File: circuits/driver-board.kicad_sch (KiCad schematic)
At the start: 59 parts, among them J1 Backpack_Conn_02x09, J2 USB4120-03-C_REVA, J3 Motor_Conn_01x04, Q1 MMBT3904, Q2 MMBT3904, SW1 ESP_EN_SW_Push, SW2 ESP_IO0_SW_Push, U1 CP2102N-A01-GQFN24, U2 BD33FC0WEFJ-E2, U3 ESP32-S3, U4 AS5601-ASOT, U5 TMC2209-LA, U6 STUSB4500QTR

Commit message: updated 3d models
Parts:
- removed U2: BD33FC0WEFJ-E2, Slimc_Converter_DCDC:BD33FC0WEFJ-E2, symbol Slimc_Converter_DCDC:BD33FC0WEFJ-E2
- added U2: BAxxXX0, Package_TO_SOT_SMD:TO-252-2, symbol Slimc_Converter_DCDC:BAxxXX0
- gave numbers to parts that had none: 1
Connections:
- net +3V3: now also U2.3 (OUT)
- net VBUS: now also U2.1 (VCC)
- new net: U2.2 (GND), U2.Fin (GND)
- no-connect marks 35 -> 30
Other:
- moved on the sheet: C3

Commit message: work on external spram and pcb layout
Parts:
- removed AE1: Antenna_Shield, symbol Device:Antenna_Shield
- removed C2: ??µF 35V, Capacitor_SMD:C_1206_3216Metric, symbol Device:CP_Small
- removed C24: 100µF-6.3V-0603, Capacitor_SMD:C_0603_1608Metric, symbol Device:CP_Small
- removed C6: 100nF, Capacitor_SMD:C_0603_1608Metric, symbol Device:CP_Small
- removed C7: 2µ2F-6.3V, Capacitor_SMD:C_0603_1608Metric, symbol Device:C_Small
- removed J1: Backpack_Conn_02x09, Connector_PinSocket_2.54mm:PinSocket_2x09_P2.54mm_Vertical, symbol Connector:Screw_Terminal_01x18
- removed J4: Barrel_Jack, symbol Connector:Barrel_Jack
- removed R3: 4K7-0402, Resistor_SMD:R_0603_1608Metric, symbol Device:R_Small
- removed SW2: ESP_IO0_SW_Push, Button_Switch_SMD:SW_SPST_B3U-1000P, symbol Switch:SW_Push
- added AE1: Antenna, Slimc_RF_Antenna:XCVR_NN01-102, symbol Device:Antenna
- added C2, C24, C26, C27, C28: 1µF-6v3, Capacitor_SMD:C_0402_1005Metric, symbol Device:C_Small
- added C29: 0.1µF-6v3, Capacitor_SMD:C_0402_1005Metric, symbol Device:C_Small
- added C6: 100nF-6v3-0603, Capacitor_SMD:C_0402_1005Metric, symbol Device:C_Small
- added J1: Conn_01x18_Female, Connector_PinSocket_2.54mm:PinSocket_2x09_P2.54mm_Vertical, symbol Connector:Conn_01x18_Female
- added J4: Screw_Terminal_01x02, TerminalBlock_Phoenix:TerminalBlock_Phoenix_MKDS-1,5-2-5.08_1x02_P5.08mm_Horizontal, symbol Connector:Screw_Terminal_01x02
- added J5: Conn_01x06_Female, Connector_PinSocket_2.54mm:PinSocket_2x03_P2.54mm_Vertical, symbol Connector:Conn_01x06_Female
- added R14: 4K7-0402, Resistor_SMD:R_0402_1005Metric, symbol Device:R_Small
- added R2: 20K-0402, Resistor_SMD:R_0402_1005Metric, symbol Device:R_Small
- added R5: 715K-0402, Resistor_SMD:R_0402_1005Metric, symbol Device:R_Small
- added R6: 110K-0402, Resistor_SMD:R_0402_1005Metric, symbol Device:R_Small
- added R9: 100K-0402, Resistor_SMD:R_0402_1005Metric, symbol Device:R_Small
- added U7: ESP-PSRAM32, Package_SO:SOIC-8_3.9x4.9mm_P1.27mm, symbol Memory_RAM:ESP-PSRAM32
- added Y1: 40Mhz, Crystal:Crystal_SMD_2016-4Pin_2.0x1.6mm, symbol Device:Crystal_GND2
- C1: value 100nF-6.3V-0603 -> 100nF-6v3-0603; footprint Capacitor_SMD:C_0603_1608Metric -> Capacitor_SMD:C_0402_1005Metric
- C10, C11, C18, C21: footprint Capacitor_SMD:C_0603_1608Metric -> Capacitor_SMD:C_0402_1005Metric
- C14, C15, C16, C17: footprint Capacitor_SMD:C_0603_1608Metric -> Capacitor_SMD:C_0402_1005Metric; now left out of the parts list
- C20: footprint (none) -> Capacitor_SMD:C_0402_1005Metric
- C25: value TBD -> 1µF-6v3; footprint (none) -> Capacitor_SMD:C_0402_1005Metric
- C3: value ??µF-0603 -> 10µF-35V-0603; footprint Capacitor_SMD:C_0603_1608Metric -> Capacitor_SMD:C_0402_1005Metric
- C4: value 10µF-0603 -> 1µF-6v3-0603; footprint Capacitor_SMD:C_0603_1608Metric -> Capacitor_SMD:C_0402_1005Metric
- C5: value 2µ2F-6.3V -> 0.1µF-6v3; footprint Capacitor_SMD:C_0603_1608Metric -> Capacitor_SMD:C_0402_1005Metric
- C9: value 2µ2F-6.3V -> 2µ2F-6v3; footprint Capacitor_SMD:C_0603_1608Metric -> Capacitor_SMD:C_0402_1005Metric
- D1: footprint Slimc_LED_SMD:WS2812_4020_SIDE -> Slimc_LED_SMD:LED_WS2812C-2020
- H1, H2, H3, H4, Q1, Q2, U1, U6: now left out of the parts list
- R1: value 4K7-0402 -> 10K-0402; footprint Resistor_SMD:R_0603_1608Metric -> Resistor_SMD:R_0402_1005Metric
- R10, R11, R4, R7, R8: footprint Resistor_SMD:R_0603_1608Metric -> Resistor_SMD:R_0402_1005Metric
- R12, R13: value 0R11-2010-1W -> 0R11-0805-1W; footprint Resistor_SMD:R_2010_5025Metric -> Resistor_SMD:R_0805_2012Metric
- R15, R16, R17: footprint Resistor_SMD:R_0603_1608Metric -> Resistor_SMD:R_0402_1005Metric; now left out of the parts list
- SW1: value ESP_EN_SW_Push -> RST_SW_Push
- U2: value BAxxXX0 -> BA33DD0T
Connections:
- net ESP_IO10 is gone; now on net AS5601_ABI_A: U3.15 (GPIO10/ADC1_CH9)
- net +3V3: now also C5.2, R1.1, R7.2, C24.2, C6.2, J5.2 (Pin_2); no longer R1.2, R7.1
- net AS5601_ABI_A: no longer R10.2, R11.1, R11.2, R7.2, R8.2, U1.20 (RXD), U1.21 (TXD), U4.5 (B), U4.6 (SDA), U4.7 (SCL), U5.11 (DIAG), U5.14 (PDN_UART), U5.16 (STEP), U5.19 (DIR), U5.2 (ENN), U6.7 (SCL), U6.8 (SDA)
- net ESP_EN: now also R1.2, SW1.2, C2.1, J5.4 (Pin_4); no longer C5.1, R1.1, SW1.1
- net ESP_IO00: now also J5.3 (Pin_3); no longer U3.52 (GPIO46)
- net ESP_IO04: now also R10.2, U4.7 (SCL), U6.7 (SCL), J1.16 (Pin_16)
- net ESP_IO05: now also R8.2, U4.6 (SDA), U6.8 (SDA), J1.15 (Pin_15)
- net ESP_IO06: now also R7.1, U5.2 (ENN), J1.14 (Pin_14)
- net ESP_IO07: now also U5.11 (DIAG), R2.1
- net ESP_IO08: now also U5.16 (STEP)
- net ESP_IO09: now also U5.19 (DIR)
- net ESP_IO14: now also J1.12 (Pin_12), R5.2, R6.1
- net ESP_IO17: now also J1.11 (Pin_11)
- net ESP_IO18: now also J1.10 (Pin_10)
- net ESP_IO19: now also J1.9 (Pin_9)
- net ESP_IO43: now also U1.21 (TXD), J5.6 (Pin_6)
- net ESP_IO44: now also U1.20 (RXD), J5.5 (Pin_5)
- net ESP_IO45: now also R11.1, J1.18 (Pin_18)
- net GND: now also C5.1, C9.2, L1.1, SW1.1, U2.2 (GND), U2.Fin (GND), C2.2, C24.1, C26.1, C27.1, C28.1, C29.1, C6.1, J1.1 (Pin_1), J1.13 (Pin_13), J1.3 (Pin_3), J1.5 (Pin_5), J4.1 (Pin_1), J5.1 (Pin_1), R14.1, R2.2, R6.2, U7.4 (VSS), Y1.2; no longer C20.2, C5.2, C9.1, SW1.2
- net VBUS: now also J1.2 (Pin_2), J1.4 (Pin_4), J1.6 (Pin_6), J4.2 (Pin_2), R5.1
- net at U5.8 (5VOUT): now also C9.1; no longer C9.2
- net at L1.2: now also C20.1, AE1.1 (A); no longer C25.2
- net ESP_SPICS1: now reaches U3.28 (SPI_CS1/GPIO26)
- net ESP_SPICS1: now also R9.2, U7.1 (~{CE})
- net ESP_SPIVDD: now reaches U3.29 (VDD_SPI)
- net ESP_SPIVDD: now also C28.2, C29.2, R9.1, U7.8 (VCC)
- net ESP_SPIHD: now reaches U3.30 (SPIHD/GPIO27)
- net ESP_SPIHD: now also U7.7 (SIO3)
- net ESP_SPIWP: now reaches U3.31 (SPIWP/GPIO28)
- net ESP_SPIWP: now also U7.3 (SIO2)
- net ESP_SPICLK: now reaches U3.33 (SPICLK/GPIO30)
- net ESP_SPICLK: now also U7.6 (SCLK)
- net ESP_SPIQ: now reaches U3.34 (SPIQ/GPIO31)
- net ESP_SPIQ: now also U7.2 (SO/SIO)
- net ESP_SPID: now reaches U3.35 (SPID/GPIO32)
- net ESP_SPID: now also U7.5 (SI/SIO)
- net at U3.37 (SPICLK_P/GPIO47): now also C27.2, R14.2
- net at U3.53 (XTAL_N): now also C26.2, Y1.3
- net at U3.54 (XTAL_P): now also C25.2, Y1.1
- net ESP_IO11 renamed AS5601_ABI_B
- net AS5601_ABI_B: now also U4.5 (B)
- new net: C20.2, U3.1 (LNA_IN/RF)
- new net ESP_IO46: J1.17 (Pin_17), R11.2, U3.52 (GPIO46), U5.14 (PDN_UART)
- no-connect marks 30 -> 20
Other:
- note added: "2) CLC filter on analog power pins https://www.espressif.com/sites/default/files/documentation/esp32-s3_hardware_design_guidelines_en.pdf#page=8"
- note added: "3) External clock https://www.espressif.com/sites/default/files/documentation/esp32-s3_hardware_design_guidelines_en.pdf#page=11"
- note added: "Delay boot ~50µS"
- note added: "MAX 25V"
- note added: "MAX 5A LOAD"
- note added: "PROGRAMMING HEADER"
- note added: "TO BE DELETED"
- note added: "USB TO UART"
- note added: "from https://dl.espressif.com/dl/SCH_ESP32-S3-DEVKITC-1_V1_20210312C.pdf"
- note removed: "USB TO UART (from https://dl.espressif.com/dl/SCH_ESP32-S3-DEVKITC-1_V1_20210312C.pdf)"
- moved on the sheet: C14, C15, C16, C17, C18, C19, C20, C21, C22, C23, C3, C4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

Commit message: couple of renders
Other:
- note removed: "1) Adding GPIO46 to reset circuitry according to TABLE 9: Strapping Pins https://www.espressif.com/sites/default/files/documentation/esp32-s3_datasheet_en.pdf#page=22"
- note removed: "2) CLC filter on analog power pins https://www.espressif.com/sites/default/files/documentation/esp32-s3_hardware_design_guidelines_en.pdf#page=8"
- note removed: "3) External clock https://www.espressif.com/sites/default/files/documentation/esp32-s3_hardware_design_guidelines_en.pdf#page=11"
- note removed: "NOTES"
- note removed: "TO BE DELETED"
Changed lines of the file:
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@@
-    (stroke (width 0) (type default) (color 0 0 0 0))
-  )
-  (polyline (pts (xy 382.27 405.13) (xy 382.27 303.53))
     (stroke (width 0) (type default) (color 0 0 0 0))
   )
@@
     (stroke (width 0) (type default) (color 0 0 0 0))
   )
-  (polyline (pts (xy 16.51 303.53) (xy 16.51 405.13))
-    (stroke (width 0) (type default) (color 0 0 0 0))
-  )
   (wire (pts (xy 173.99 59.055) (xy 173.99 77.47))
     (stroke (width 0) (type default) (color 0 0 0 0))
@@
   )
   (wire (pts (xy 230.505 264.16) (xy 234.95 264.16))
-    (stroke (width 0) (type default) (color 0 0 0 0))
-  )
-  (polyline (pts (xy 16.51 405.13) (xy 382.27 405.13))
     (stroke (width 0) (type default) (color 0 0 0 0))
   )
@@
   )
   (text "MAX 5A LOAD" (at 471.805 203.835 90)
-    (effects (font (size 1.27 1.27)) (justify left bottom))
-  )
-  (text "NOTES" (at 17.78 307.34 0)
     (effects (font (size 1.27 1.27)) (justify left bottom))
   )
@@
     (effects (font (size 2.54 2.54) (thickness 0.508) bold) (justify left bottom))
   )
-  (text "1) Adding GPIO46 to reset circuitry according to TABLE 9: Strapping Pins https://www.espressif.com/sites/default/files/documentation/esp32-s3_datasheet_en.pdf#page=22"
-    (at 20.32 312.42 0)
-    (effects (font (size 1.27 1.27)) (justify left bottom))
-  )
   (text "STATUS LED" (at 383.54 85.725 0)
     (effects (font (size 2.54 2.54) (thickness 0.508) bold) (justify left bottom))
   )
-  (text "2) CLC filter on analog power pins https://www.espressif.com/sites/default/files/documentation/esp32-s3_hardware_design_guidelines_en.pdf#page=8"
-    (at 20.32 316.23 0)
-    (effects (font (size 1.27 1.27)) (justify left bottom))
-  )
   (text "STEPPER CONTROL" (at 158.115 22.86 0)
     (effects (font (size 2.54 2.54) (thickness 0.508) bold) (justify left bottom))
@@
     (effects (font (size 2.54 2.54) (thickness 0.508) bold) (justify left bottom))
   )
-  (text "TO BE DELETED" (at 384.175 309.245 0)
-    (effects (font (size 2.54 2.54) (thickness 0.508) bold) (justify left bottom))
-  )
-  (text "3) External clock https://www.espressif.com/sites/default/files/documentation/esp32-s3_hardware_design_guidelines_en.pdf#page=11"
-    (at 20.32 320.04 0)
-    (effects (font (size 1.27 1.27)) (justify left bottom))
-  )
   (text "Delay boot ~50µS" (at 211.455 197.485 0)

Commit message: adjusting schematic and pcb component placement
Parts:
- removed C24: 1µF-6v3, Capacitor_SMD:C_0402_1005Metric, symbol Device:C_Small
- removed Q1, Q2: MMBT3904, Package_TO_SOT_SMD:SOT-23, symbol Transistor_BJT:MMBT3904
- removed Y1: 40Mhz, Crystal:Crystal_SMD_2016-4Pin_2.0x1.6mm, symbol Device:Crystal_GND2
- added C30: 1µF, Capacitor_SMD:C_0402_1005Metric, symbol Device:C_Small
- added C31, C32, C33: 100nF, Capacitor_SMD:C_0402_1005Metric, symbol Device:C_Small
- added C34: 1pF, Capacitor_SMD:C_0402_1005Metric, symbol Device:C_Small
- added C35: 15pF, Capacitor_SMD:C_0402_1005Metric, symbol Device:C_Small
- added C7: 10nF, Capacitor_SMD:C_0402_1005Metric, symbol Device:C_Small
- added Q1, Q2: SS8050-G, Package_TO_SOT_SMD:SOT-23, symbol Device:Q_NPN_BEC
- added R3: 20K, Resistor_SMD:R_0402_1005Metric, symbol Device:R_Small
- added U8: 74LVC2G00, Package_SON:X2SON-8_1.4x1mm_P0.35mm, symbol 74xGxx:74LVC2G00
- added Y1: 40MHz, Crystal:Crystal_SMD_2016-4Pin_2.0x1.6mm, symbol Device:Crystal_GND24
- AE1: symbol Device:Antenna -> Device:Antenna_Shield
- C1, C6: value 100nF-6v3-0603 -> 100nF
- C12, C13: value 100nF-16V -> 100nF
- C18: value 100nF-25V -> 100nF
- C2, C27, C28: value 1µF-6v3 -> 1µF
- C20: value TBD -> NC
- C21: value 100nF-50V-0603 -> 100nF-50V
- C22, C23: value 10µF-50V-2220 -> 10µF-50V
- C25: value 1µF-6v3 -> 10µF
- C26: value 1µF-6v3 -> 15pF
- C29: value 0.1µF-6v3 -> 100nF
- C3: value 10µF-35V-0603 -> 10µF-35V
- C4: value 1µF-6v3-0603 -> 1µF
- C5: value 0.1µF-6v3 -> 1µF
- D3: value SMB28A -> SMB24A; footprint Diode_SMD:D_SMB -> Diode_SMD:D_1210_3225Metric
- J4: value Screw_Terminal_01x02 -> Screw_Terminals
- L1: value TBD -> 0R; footprint (none) -> Resistor_SMD:R_0402_1005Metric
- R1, R15: value 10K-0402 -> 10K
- R10, R14, R8: value 4K7-0402 -> 4K7
- R11: value 1K-1%-0603 -> 1K-1%
- R16, R17: value 10K-0603 -> 10K
- R2, R7: value 20K-0402 -> 20K
- R4: value 230R-0402 -> 230
- R5: value 715K-0402 -> 715K
- R6: value 110K-0402 -> 110K
- R9: value 100K-0402 -> 100K
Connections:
- net ESP_IO12 is gone; now on net AS5601_ABI_B: U3.17 (GPIO12/ADC2_CH1)
- net ESP_IO20 is gone; now on net USB_D+: U3.26 (GPIO20/USB_D+/ADC2_CH9)
- net ESP_IO48 is gone; now on net ESP_IO01: R4.1
- net +3V3: now also C25.2, C30.2, C31.2, C32.2, C33.2, C7.2, R3.1, U8.8 (VCC), U8.8 (VCC)
- net AS5601_ABI_A: now also U3.16 (GPIO11/ADC2_CH0); no longer U3.15 (GPIO10/ADC1_CH9)
- net AS5601_ABI_B: no longer U3.16 (GPIO11/ADC2_CH0)
- net ESP_EN: now also Q1.3 (C)
- net ESP_IO00: now also Q2.3 (C)
- net ESP_IO02: now also J1.8 (Pin_8)
- net ESP_IO03: now also J1.7 (Pin_7)
- net ESP_IO07: now also U5.16 (STEP); no longer R2.1, U5.11 (DIAG)
- net ESP_IO08: now also U5.19 (DIR); no longer U5.16 (STEP)
- net ESP_IO09: now also U8.5, U8.7; no longer U5.19 (DIR)
- net ESP_IO19: no longer U3.25 (GPIO19/USB_D-/ADC2_CH8)
- net ESP_IO44: no longer U3.50 (U0RXD/PROG/GPIO44)
- net GND: now also AE1.2 (Shield), C20.2, C30.1, C31.1, C32.1, C33.1, C34.2, C35.1, C7.1, U8.4 (GND), U8.4 (GND), Y1.2, Y1.4; no longer L1.1
- net USB_D-: now also U3.25 (GPIO19/USB_D-/ADC2_CH8)
- net CP2102_DTR: now reaches R16.1
- net CP2102_DTR: now also U1.23 (DTR), Q2.2 (E); no longer U1.19 (RTS)
- net CP2102_RTS: now reaches R17.1
- net CP2102_RTS: now also U1.19 (RTS), Q1.2 (E); no longer U1.23 (DTR)
- net at R17.2: now also Q2.1 (B)
- net at R16.2: now also Q1.1 (B)
- net at C20.1, L1.2: now also U3.1 (LNA_IN/RF); no longer AE1.1 (A)
- net ESP_XTAL_N: now reaches C26.2, U3.53 (XTAL_N)
- net ESP_XTAL_N: now also Y1.3
- net ESP_XTAL_P: now reaches U3.54 (XTAL_P)
- net ESP_XTAL_P: now also C35.2, Y1.1; no longer C25.2
- net ESP_IO15: no longer names the net of U3.21 (GPIO15/ADC2_CH4/XTAL_32K_P)
- net ESP_IO16: no longer names the net of U3.22 (GPIO16/ADC2_CH5/XTAL_32K_N)
- net ESP_IO33: no longer names the net of U3.38 (GPIO33)
- net ESP_IO34: no longer names the net of U3.39 (GPIO34)
- net ESP_IO35: no longer names the net of U3.40 (GPIO35)
- net ESP_IO36: no longer names the net of U3.41 (GPIO36)
- net ESP_IO37: no longer names the net of U3.42 (GPIO37)
- net ESP_IO38: no longer names the net of U3.43 (GPIO38)
- net ESP_IO39: no longer names the net of U3.44 (MTCK/JTAG/GPIO39)
- net ESP_IO40: no longer names the net of U3.45 (MTDO/JTAG/GPIO40)
- net ESP_IO41: no longer names the net of U3.47 (MTDI/JTAG/GPIO41)
- net ESP_IO42: no longer names the net of U3.48 (MTMS/JTAG/GPIO42)
- new net: AE1.1 (A), C34.1, L1.1
- new net: U8.2, U8.3
- new net ESP_IO10: R3.2, U3.15 (GPIO10/ADC1_CH9), U8.6
- new net TMC2209_DIAG: R2.1, U5.11 (DIAG), U8.1
- no-connect marks 20 -> 32
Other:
- note added: "LET STUSB4500 enable BA33DD0T?"
- note added: "Program Sequence DTR RTS --> EN IO00 1 1 1 1 0 0 1 1 1 0 0 1 0 1 1 0"
- note added: "USB-UART BRIDGE"
- note removed: "USB TO UART"
- moved on the sheet: C12, C13, C20, C26, C27, C3, C4, H1, H2, H3, H4, J1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

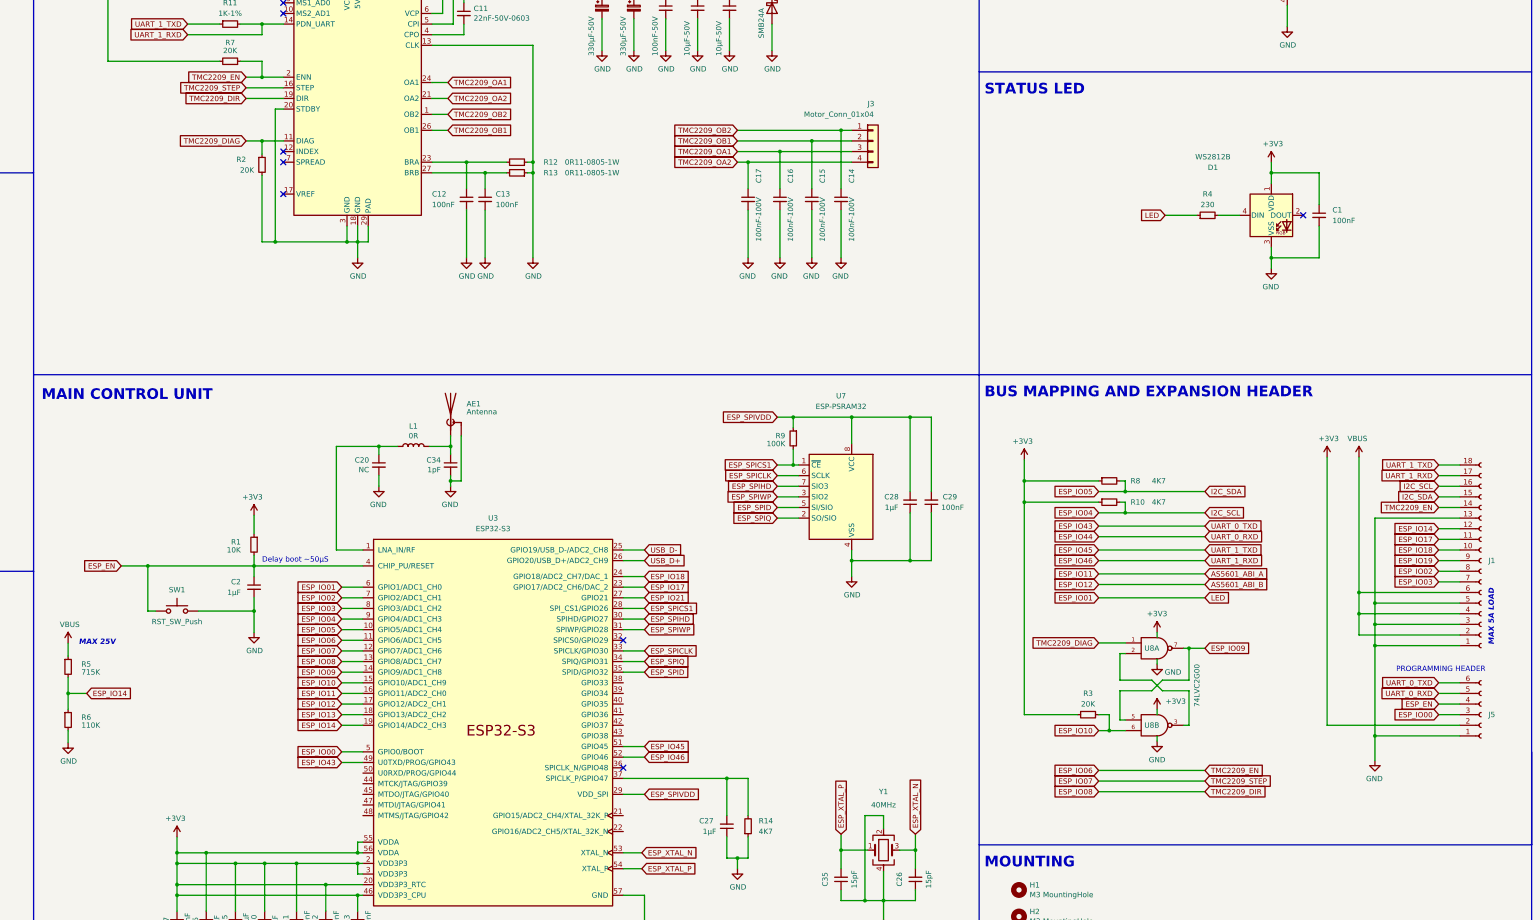
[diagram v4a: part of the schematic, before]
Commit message: tmc2209 -> tmc 2226
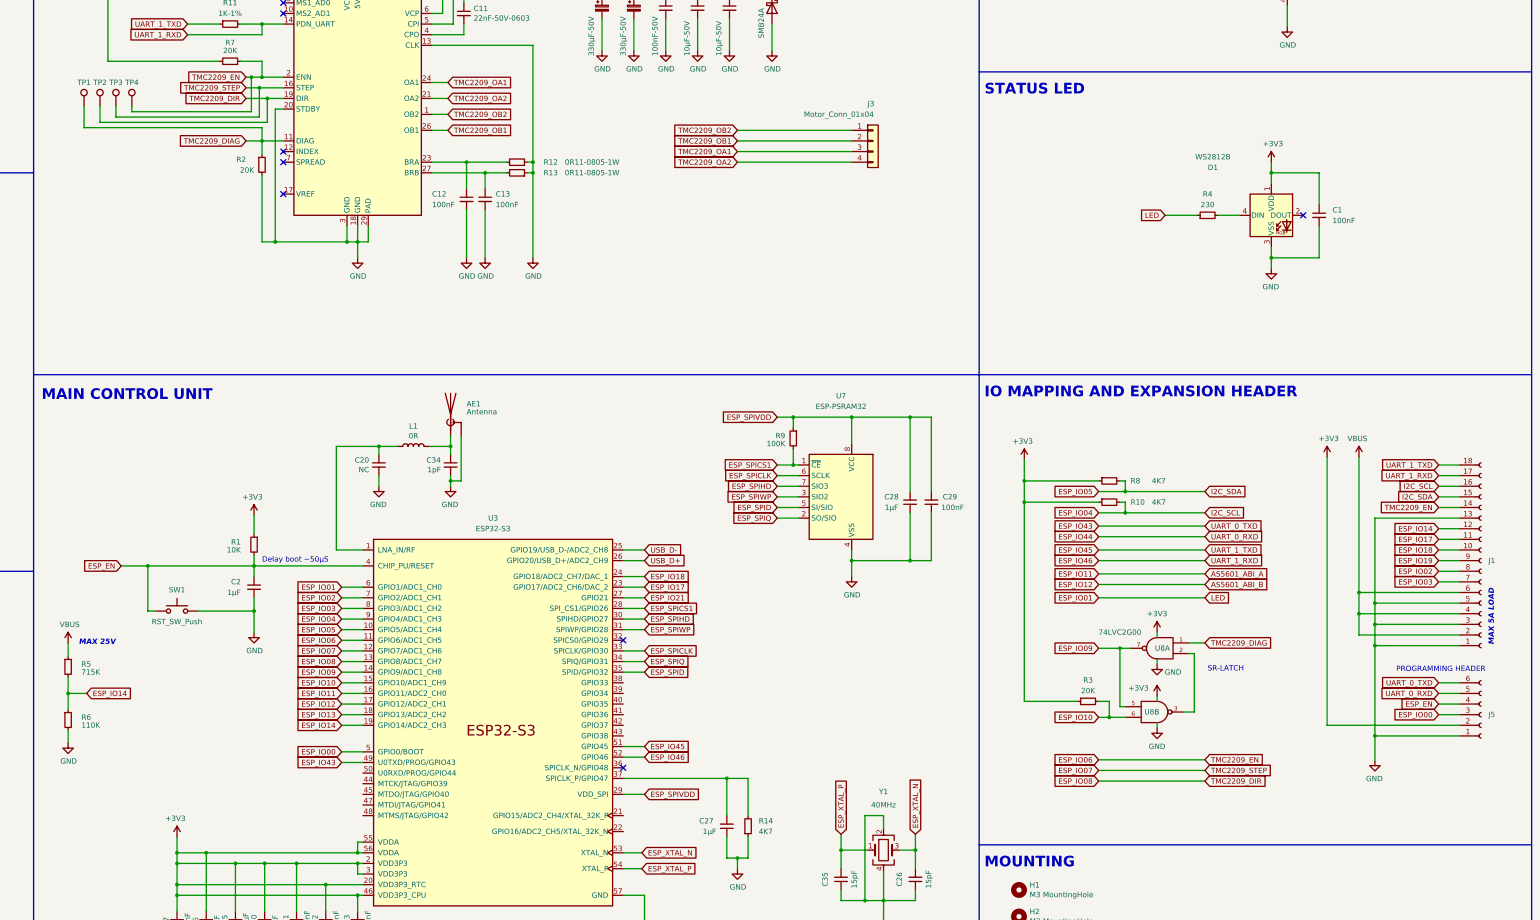
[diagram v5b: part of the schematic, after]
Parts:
- removed C14, C15, C16, C17: 100nF-100V, Capacitor_SMD:C_0402_1005Metric, symbol Device:C_Small
- added TP1, TP2, TP3, TP4: TestPoint, symbol Connector:TestPoint
- U5: footprint Package_DFN_QFN:QFN-28-1EP_5x5mm_P0.5mm_EP3.35x3.35mm_ThermalVias -> Package_SO:HTSSOP-28-1EP_4.4x9.7mm_P0.65mm_EP3.4x9.5mm_ThermalVias
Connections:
- net ESP_IO06: now also TP4.1
- net ESP_IO07: now also TP3.1
- net ESP_IO08: now also TP2.1
- net TMC2209_DIAG: now also TP1.1
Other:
- note added: "IO MAPPING AND EXPANSION HEADER"
- note added: "SR-LATCH"
- note removed: "BUS MAPPING AND EXPANSION HEADER"
- moved on the sheet: R3, U8A, U8B

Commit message: date marker
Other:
- company: slimc -> (none)
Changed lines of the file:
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@@
   (title_block
     (title "esp-stepper-servo")
-    (date "2022-04-28")
+    (date "%%date%%")
     (rev "v0.0.1")
-    (company "slimc")
     (comment 1 "github.com/slimcdk/esp-stepper-servo")
   )

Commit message: workflow kibot generate schematics with text replace
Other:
- title: esp-stepper-servo -> ESP Stepper Servo
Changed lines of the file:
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@@
   (paper "A2")
   (title_block
-    (title "esp-stepper-servo")
-    (date "%%date%%")
-    (rev "v0.0.1")
-    (comment 1 "github.com/slimcdk/esp-stepper-servo")
+    (title "ESP Stepper Servo")
+    (date "${date}")
+    (rev "${version}")
+    (comment 1 "github.com/slimcdk/esp-stepper-servo/tree/${commit_long}")
+    (comment 2 "github.com/slimcdk/esp-stepper-servo")
   )
   (junction (at 204.47 269.24) (diameter 0) (color 0 0 0 0)
